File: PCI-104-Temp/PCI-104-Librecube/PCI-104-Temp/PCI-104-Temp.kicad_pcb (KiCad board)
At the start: 2 copper layers, 95.9 x 90.2 mm, 6 parts, among them J3 Conn_02x26_Row_Letter_First, J4 Conn_02x26_Row_Letter_First

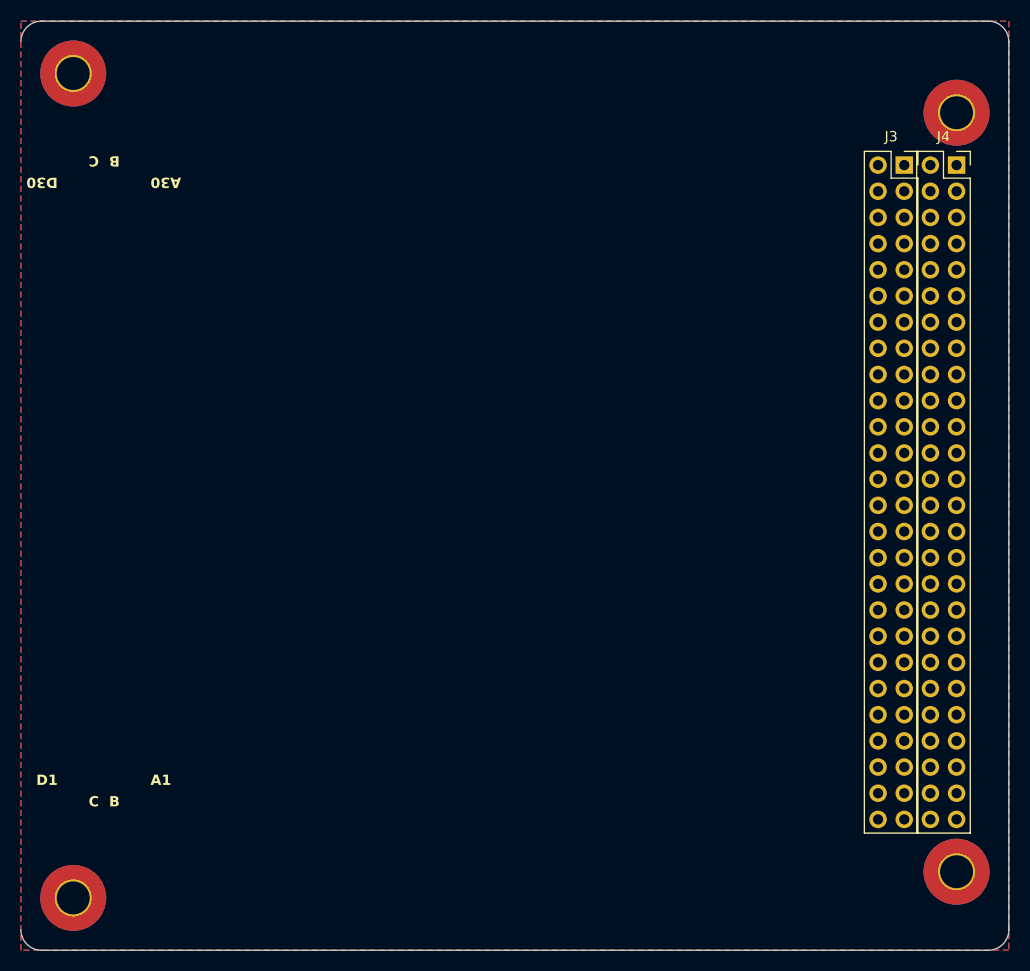
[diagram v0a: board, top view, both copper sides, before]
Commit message: PC-104 Template Upadte
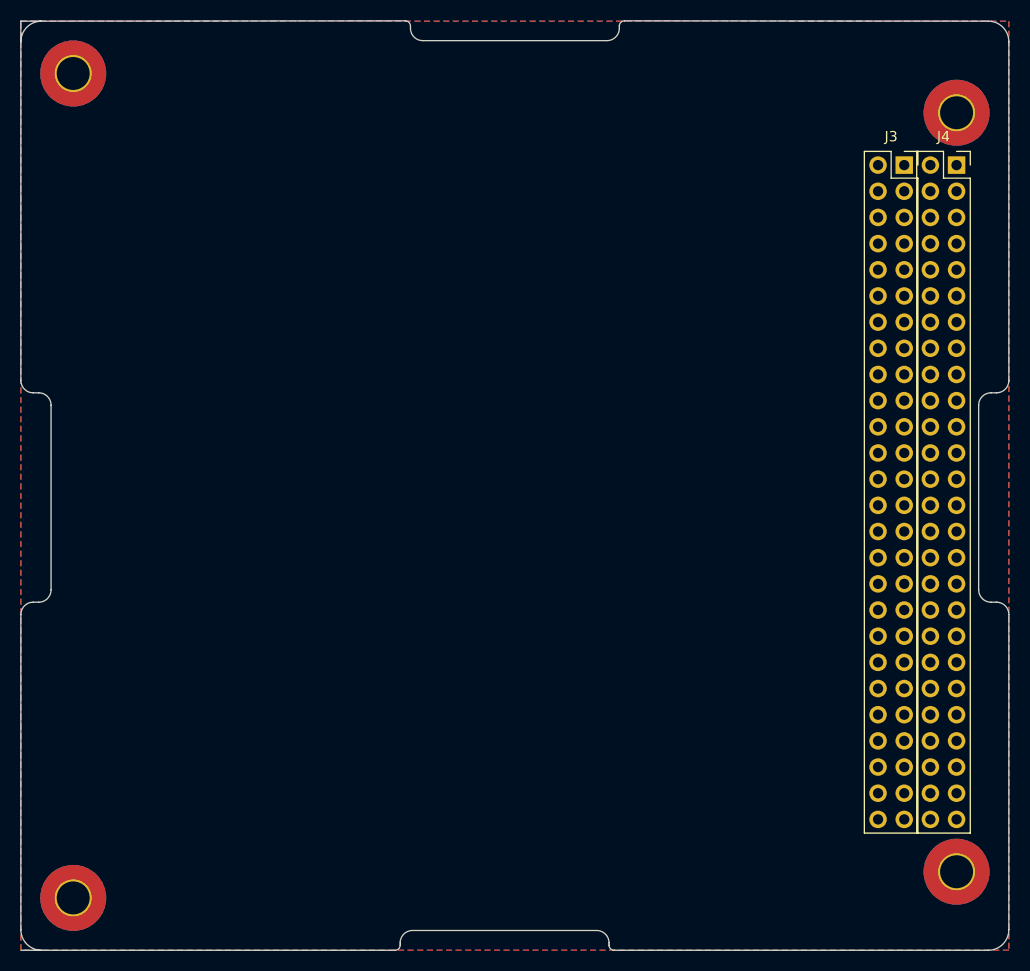
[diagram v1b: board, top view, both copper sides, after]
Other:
- outline, holes or cut-outs redrawn
- board text removed: "A1"
- board text removed: "A30"
- board text removed: "B"
- board text removed: "C"
- board text removed: "D1"
- board text removed: "D30"

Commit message: PC104 Template Updates
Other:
- outline, holes or cut-outs redrawn
